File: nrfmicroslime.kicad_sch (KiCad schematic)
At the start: 21 parts, among them J1 Conn_01x13_Pin, J2 Conn_01x13_Pin, J3 532610271, SW1 TS-1088-AR02016, U1 ICM-42688-V, U2 LIS2MDL, X1 S2D32.768KB20F30T

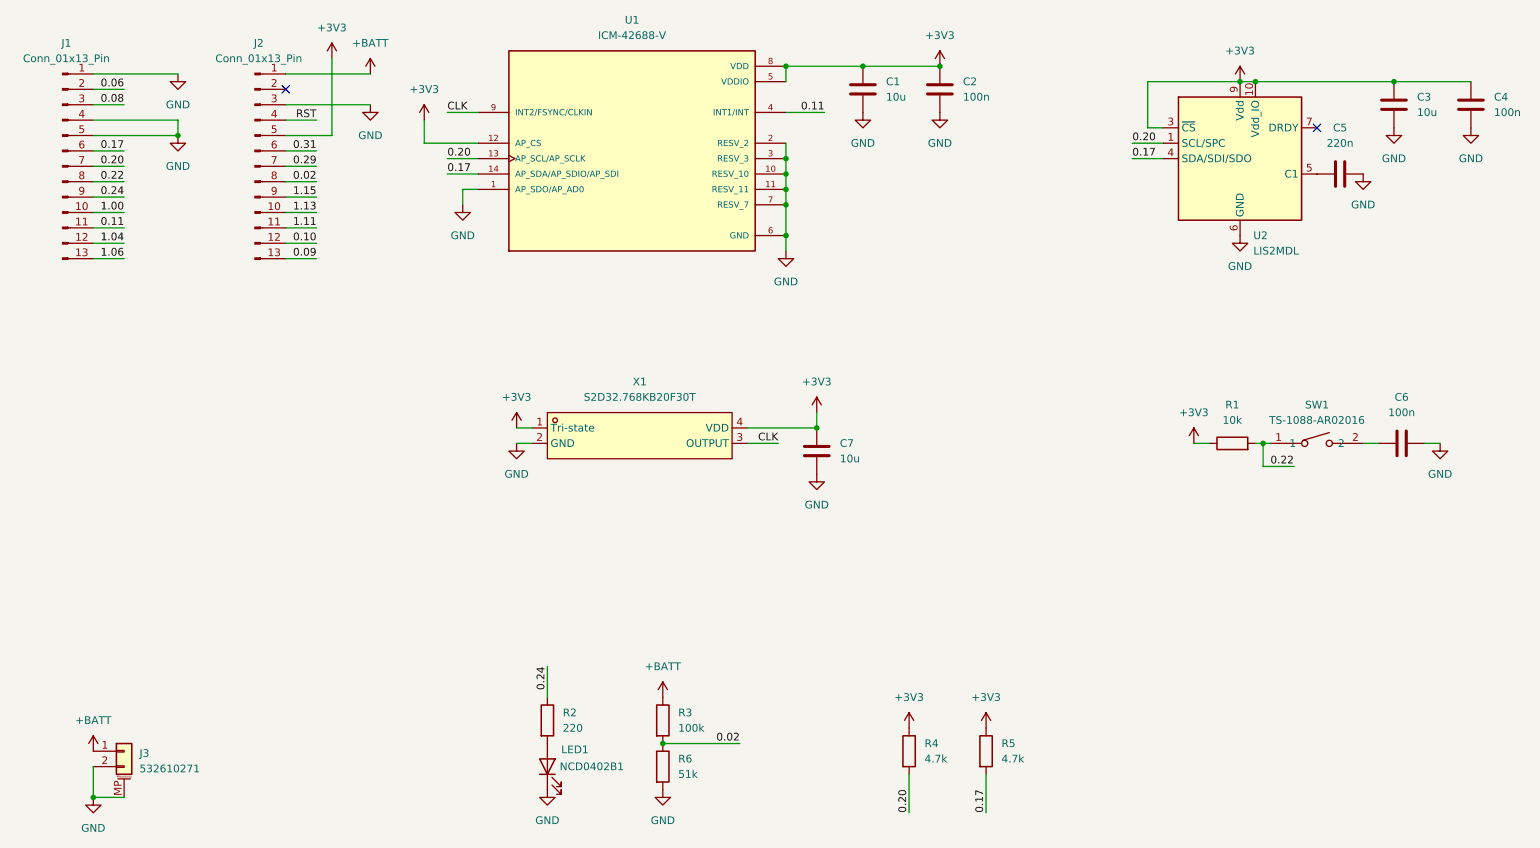
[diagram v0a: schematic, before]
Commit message: narrower pcb, less components, pin configuration change
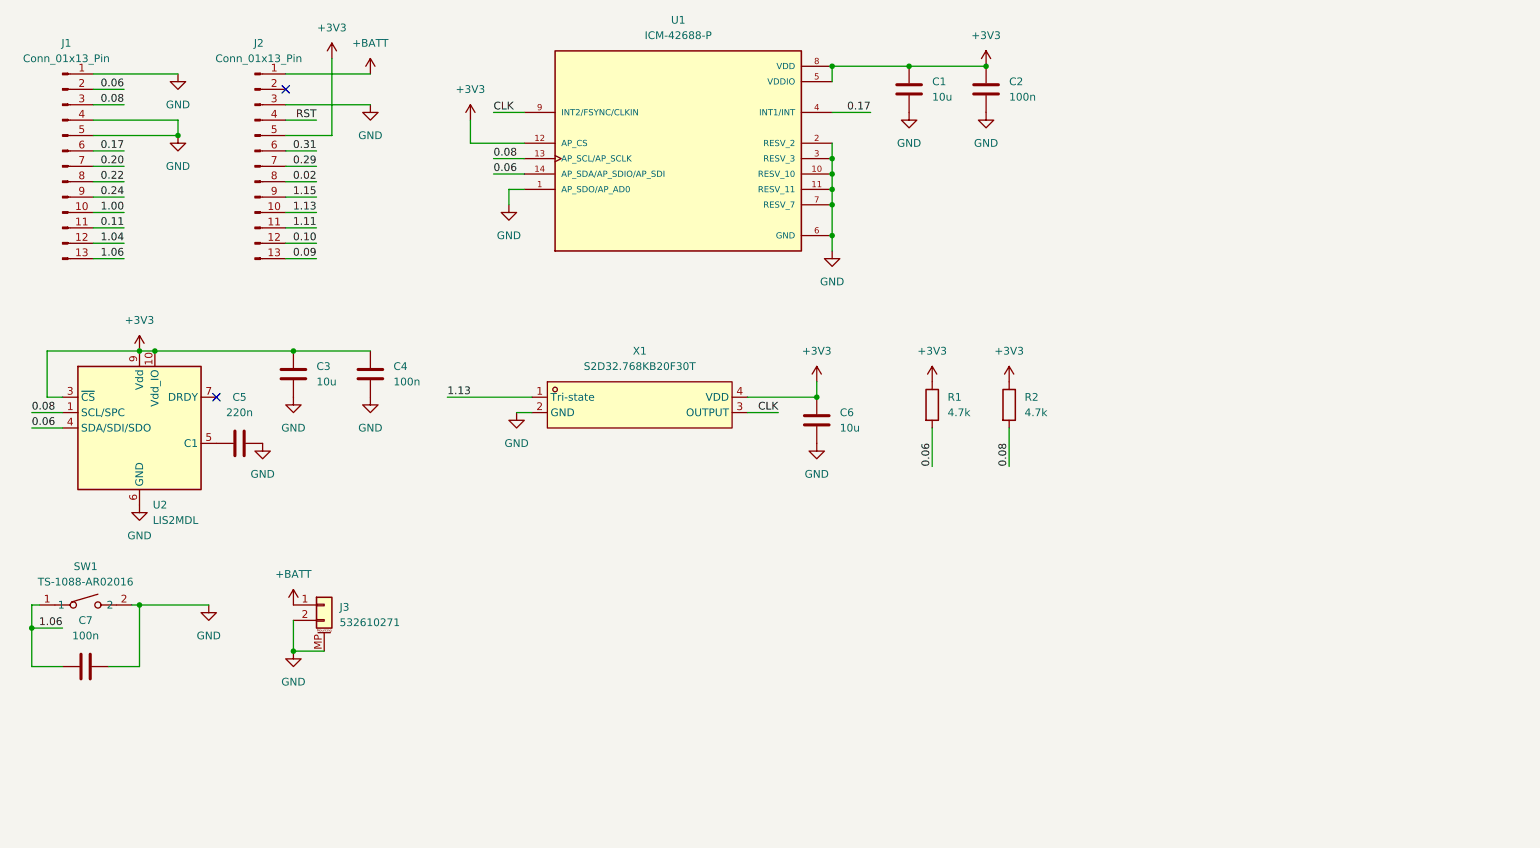
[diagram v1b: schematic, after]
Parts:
- removed C6: 100n, Capacitor_SMD:C_0402_1005Metric, symbol Device:C
- removed LED1: NCD0402B1, LED_SMD:LED_0402_1005Metric, symbol Device:LED
- removed R1: 10k, Resistor_SMD:R_0402_1005Metric, symbol Device:R
- removed R2: 220, Resistor_SMD:R_0402_1005Metric, symbol Device:R
- removed R3: 100k, Resistor_SMD:R_0402_1005Metric, symbol Device:R
- removed R6: 51k, Resistor_SMD:R_0402_1005Metric, symbol Device:R
- added C7: 100n, Capacitor_SMD:C_0402_1005Metric, symbol Device:C
- U1: value ICM-42688-V -> ICM-42688-P
- renumbered C7 to C6, R4 to R1, R5 to R2
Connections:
- net +3V3: no longer X1.1 (Tri-state)
- net 0.06: now also R1.2, U1.14 (AP_SDA/AP_SDIO/AP_SDI), U2.4 (SDA/SDI/SDO)
- net 0.08: now also R2.2, U1.13 (AP_SCL/AP_SCLK), U2.1 (SCL/SPC)
- net 0.11: no longer U1.4 (INT1/INT)
- net 0.17: now also U1.4 (INT1/INT); no longer R2.2, U1.14 (AP_SDA/AP_SDIO/AP_SDI), U2.4 (SDA/SDI/SDO)
- net 0.20: no longer R1.2, U1.13 (AP_SCL/AP_SCLK), U2.1 (SCL/SPC)
- net 0.22: no longer SW1.1
- net 1.06: now also SW1.1, C7.1
- net 1.13: now also X1.1 (Tri-state)
- net GND: now also SW1.2, C7.2
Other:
- moved on the sheet: C1, C2, C3, C4, C5, C6, J3, R1, R2, SW1, U1, U2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
